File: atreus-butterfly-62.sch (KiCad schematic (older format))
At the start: 78 parts

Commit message: switch to serial comms
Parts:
- removed C?: 1u, symbol C_Small
- removed C?: 10u, symbol C_Small
- removed R? (x3): 4k7, symbol R_Small
- removed U?: MCP23017, symbol MCP23017
- added J?: Conn_01x04, symbol Conn_01x04
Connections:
- net labels added: Rx, Tx
- net labels removed: SCL, SDA
- wire segments 94 -> 80
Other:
- moved on the sheet: D?, SW?

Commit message: thingy
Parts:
- added D32: D, Diodes_SMD:D_SOD-123, symbol D
- added R4: 0, Resistors_SMD:R_0603_HandSoldering, symbol R_Small
- added SW32: SW_Push, ourglass_v7:Kailh_low_profile, symbol SW_Push
- C1, C2, C3, C4: renamed from C?; footprint (none) -> Capacitors_SMD:C_0805
- D1, D10, D11, D12, D13, D14, D15, D16, D17, D18, D19, D2, D20, D21, D22, D23, D24, D25, D26, D27, D28, D29, D3, D30, D31, D4, D5, D6, D7, D8, D9: renamed from D?; footprint (none) -> Diodes_SMD:D_SOD-123
- J1: renamed from J?; footprint (none) -> Connectors:USB_Micro-B
- J2: renamed from J?; footprint (none) -> Pin_Headers:Pin_Header_Straight_1x04_Pitch2.54mm
- R1, R2, R3: renamed from R?; footprint (none) -> Resistors_SMD:R_0603_HandSoldering
- SW1, SW10, SW11, SW12, SW13, SW14, SW15, SW16, SW17, SW18, SW19, SW2, SW20, SW21, SW22, SW23, SW24, SW25, SW26, SW27, SW28, SW29, SW3, SW30, SW31, SW4, SW5, SW6, SW7, SW8, SW9: renamed from SW?; footprint (none) -> ourglass_v7:Kailh_low_profile
- U1: renamed from U?; footprint QFN44 -> ourglass_v7:QFN_44
- Y1: renamed from Y?; footprint (none) -> ourglass_v7:crystal_butterfly
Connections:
- net Column_5: now also U1.12 ((OC0A/OC1C/~RTS~/PCINT7)PB7); no longer U1.28 ((ADC11/PCINT4)PB4)
- net Column_6: now also U1.18 ((OC0B/SCL/INT0)PD0); no longer U1.29 ((ADC12/OC1A/~OC4B~/PCINT12)PB5)
- net Column_7: now also U1.19 ((SDA/INT1)PD1), D32.1 (K); no longer U1.30 ((ADC13/OC1B/OC4B/PCINT13)PB6)
- net GND: now also J1.6 (Shield)
- net Row_1: now also SW11.1, U1.22 ((XCK1/~CTS~)PD5); no longer U1.12 ((OC0A/OC1C/~RTS~/PCINT7)PB7)
- net Row_2: now also U1.25 ((ICP2/ADC8)PD4); no longer U1.31 ((OC3A/~OC4A~)PC6)
- net Row_3: now also U1.26 ((T1/~OC4D~/ADC9)PD6); no longer U1.32 ((ICP3/CLK0/OC4A)PC7)
- net Row_4: now also U1.27 ((T0/OC4D/ADC10)PD7), SW32.1; no longer U1.25 ((ICP2/ADC8)PD4)
- net Row_5: now also SW20.1, SW25.1, U1.28 ((ADC11/PCINT4)PB4); no longer U1.22 ((XCK1/~CTS~)PD5)
- net at U1.40 ((ADC1)PF1): now also R4.2
- net at U1.41 ((ADC0)PF0): now also R4.1
- net at J1.3 (D+): now also R1.2
- new net: D32.2 (A), SW32.2

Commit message: save again
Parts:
- C1, C2, C3, C4: symbol C_Small -> device:C_Small
- D1, D10, D11, D12, D13, D14, D15, D16, D17, D18, D19, D2, D20, D21, D22, D23, D24, D25, D26, D27, D28, D29, D3, D30, D31, D32, D4, D5, D6, D7, D8, D9: symbol D -> device:D
- J1: symbol USB_OTG -> atreus-butterfly-62-rescue:USB_OTG
- J2: symbol Conn_01x04 -> atreus-butterfly-62-rescue:Conn_01x04
- R1, R2, R3, R4: symbol R_Small -> device:R_Small
- SW1, SW10, SW11, SW12, SW13, SW14, SW15, SW16, SW17, SW18, SW19, SW2, SW20, SW21, SW22, SW23, SW24, SW25, SW26, SW27, SW28, SW29, SW3, SW30, SW31, SW32, SW4, SW5, SW6, SW7, SW8, SW9: symbol SW_Push -> Switch:SW_Push
- U1: symbol ATMEGA32U4-MU -> atreus-butterfly-62-rescue:ATMEGA32U4-MU
- Y1: symbol Crystal -> device:Crystal

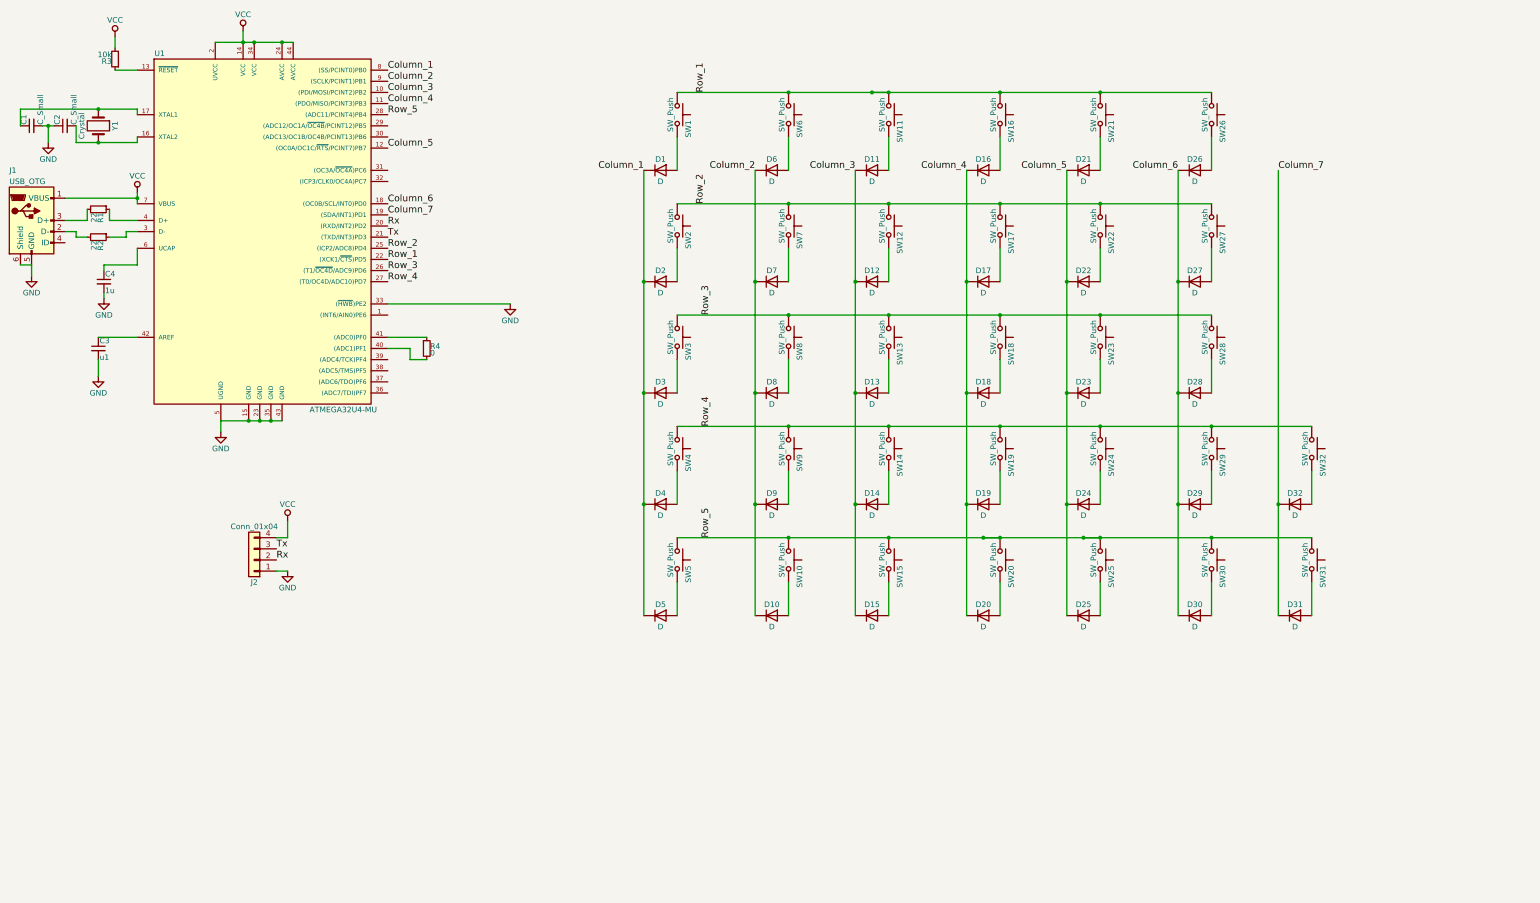
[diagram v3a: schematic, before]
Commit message: delete middle keys and most traces
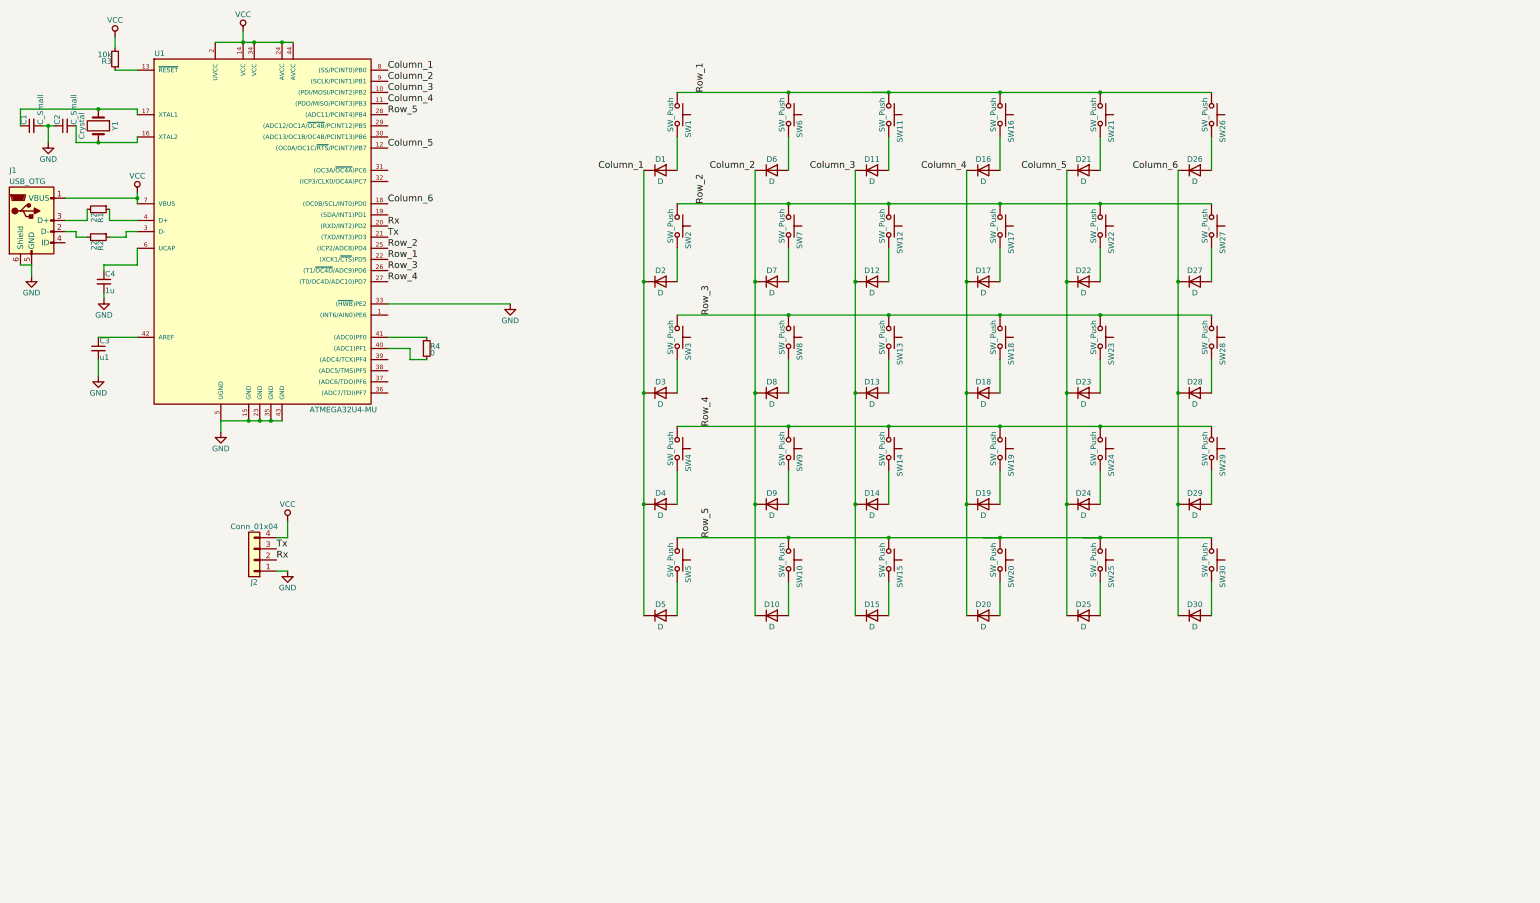
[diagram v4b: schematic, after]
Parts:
- removed D31, D32: D, Diodes_SMD:D_SOD-123, symbol device:D
- removed SW31, SW32: SW_Push, ourglass_v7:Kailh_low_profile, symbol Switch:SW_Push
- U1: footprint ourglass_v7:QFN_44 -> Housings_DFN_QFN:QFN-44-1EP_7x7mm_Pitch0.5mm
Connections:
- net Column_7: no longer names the net of U1.19 ((SDA/INT1)PD1)
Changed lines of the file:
@@
 F 0 "U1" H 2250 4500 50  0000 C CNN
 F 1 "ATMEGA32U4-MU" H 3900 1300 50  0000 C CNN
-F 2 "ourglass_v7:QFN_44" H 3200 2800 50  0001 C CIN
+F 2 "Housings_DFN_QFN:QFN-44-1EP_7x7mm_Pitch0.5mm" H 3200 2800 50  0001 C CIN
 F 3 "" H 4300 3900 50  0001 C CNN
 	1    3200 2800
@@
 Connection ~ 11400 4150
 Connection ~ 11400 5150
-Connection ~ 11700 4450
-Connection ~ 11700 5450
-$Comp
-L Switch:SW_Push SW31
-U 1 1 5C5842CF
-P 12600 5650
-F 0 "SW31" H 12650 5750 50  0000 L CNN
-F 1 "SW_Push" H 12600 5590 50  0000 C CNN
-F 2 "ourglass_v7:Kailh_low_profile" H 12600 5850 50  0001 C CNN
-F 3 "" H 12600 5850 50  0001 C CNN
-	1    12600 5650
-	0    1    1    0
-$EndComp
-$Comp
-L device:D D31
-U 1 1 5C5842D5
-P 12450 6150
-F 0 "D31" H 12450 6250 50  0000 C CNN
-F 1 "D" H 12450 6050 50  0000 C CNN
-F 2 "Diodes_SMD:D_SOD-123" H 12450 6150 50  0001 C CNN
-F 3 "" H 12450 6150 50  0001 C CNN
-	1    12450 6150
-	1    0    0    -1
-$EndComp
-Wire Wire Line
-	12600 5850 12600 6150
 Connection ~ 10700 1450
 Connection ~ 10700 2450
 Connection ~ 10700 3450
 Connection ~ 10700 4450
-Wire Wire Line
-	12300 2150 12300 5150
 Text Label 6600 2150 2    60   ~ 0
 Column_1
@@
 Text Label 11400 2150 2    60   ~ 0
 Column_6
-Text Label 4300 2550 0    60   ~ 0
-Column_7
-Text Label 12300 2150 0    60   ~ 0
-Column_7
 Connection ~ 8800 2450
 Connection ~ 8800 3450
@@
 Wire Wire Line
 	3300 5750 3400 5750
-Connection ~ 9650 5450
 Connection ~ 9800 5450
-Connection ~ 10550 5450
 Connection ~ 10700 5450
-Connection ~ 8650 1450
 Connection ~ 8800 1450
 Wire Wire Line
 	1400 2600 1600 2600
-$Comp
-L Switch:SW_Push SW32
-U 1 1 5C5B3E5C
-P 12600 4650
-F 0 "SW32" H 12650 4750 50  0000 L CNN
-F 1 "SW_Push" H 12600 4590 50  0000 C CNN
-F 2 "ourglass_v7:Kailh_low_profile" H 12600 4850 50  0001 C CNN
-F 3 "" H 12600 4850 50  0001 C CNN
-	1    12600 4650
-	0    1    1    0
-$EndComp
-$Comp
-L device:D D32
-U 1 1 5C5B3E62
-P 12450 5150
-F 0 "D32" H 12450 5250 50  0000 C CNN
-F 1 "D" H 12450 5050 50  0000 C CNN
-F 2 "Diodes_SMD:D_SOD-123" H 12450 5150 50  0001 C CNN
-F 3 "" H 12450 5150 50  0001 C CNN
-	1    12450 5150
-	1    0    0    -1
-$EndComp
-Wire Wire Line
-	12600 4850 12600 5150
-Connection ~ 12300 5150
 $Comp
 L device:R_Small R4
@@
 	11400 5150 11400 6150
 Wire Wire Line
-	11700 4450 12600 4450
-Wire Wire Line
-	11700 5450 12600 5450
-Wire Wire Line
 	10700 1450 11700 1450
 Wire Wire Line
@@
 	8800 4450 9800 4450
 Wire Wire Line
+	10700 5450 11700 5450
+Wire Wire Line
+	8800 1450 9800 1450
+Wire Wire Line
 	9650 5450 9800 5450
 Wire Wire Line
 	10550 5450 10700 5450
 Wire Wire Line
-	10700 5450 11700 5450
-Wire Wire Line
 	8650 1450 8800 1450
 Wire Wire Line
-	8800 1450 9800 1450
-Wire Wire Line
-	12300 5150 12300 6150
-Wire Wire Line
 	8800 5450 9800 5450

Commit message: no middle keys
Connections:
- wire segments 134 -> 136
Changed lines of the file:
@@
 	1    0    0    -1
 $EndComp
-Text Label 4300 1250 0    60   ~ 0
+Text Label 4300 1950 0    60   ~ 0
 Column_1
-Text Label 4300 1350 0    60   ~ 0
+Text Label 4300 1550 0    60   ~ 0
 Column_2
 Text Label 4300 1450 0    60   ~ 0
 Column_3
-Text Label 4300 1550 0    60   ~ 0
+Text Label 4300 1350 0    60   ~ 0
 Column_4
-Text Label 4300 1950 0    60   ~ 0
+Text Label 4300 1250 0    60   ~ 0
 Column_5
 Text Label 4300 2450 0    60   ~ 0
 Column_6
-Text Label 4300 2950 0    60   ~ 0
+Text Label 4300 2850 0    60   ~ 0
 Row_1
-Text Label 4300 2850 0    60   ~ 0
+Text Label 4300 3050 0    60   ~ 0
 Row_2
-Text Label 4300 3050 0    60   ~ 0
+Text Label 4300 3150 0    60   ~ 0
 Row_3
-Text Label 4300 3150 0    60   ~ 0
+Text Label 4300 1650 0    60   ~ 0
 Row_4
-Text Label 4300 1650 0    60   ~ 0
+Text Label 4300 1750 0    60   ~ 0
 Row_5
 Wire Wire Line
@@
 Wire Wire Line
 	7900 1450 8800 1450
+Wire Wire Line
+	3500 4350 3350 4350
+Wire Wire Line
+	3350 4350 3350 4400
+Connection ~ 3350 4400
 $EndSCHEMATC
